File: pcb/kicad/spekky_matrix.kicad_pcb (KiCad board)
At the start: 2 copper layers, 153 x 95.8 mm, 330 parts, among them J1 USB_B_Micro, J2 Conn_ARM_JTAG_SWD_10, Q1 DMP3125L-7, Q2 DMP3125L-7, Q3 DMP3125L-7, Q4 DMP3125L-7, Q5 DMP3125L-7, Q6 DMP3125L-7, Q7 DMP3125L-7, Q8 DMP3125L-7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

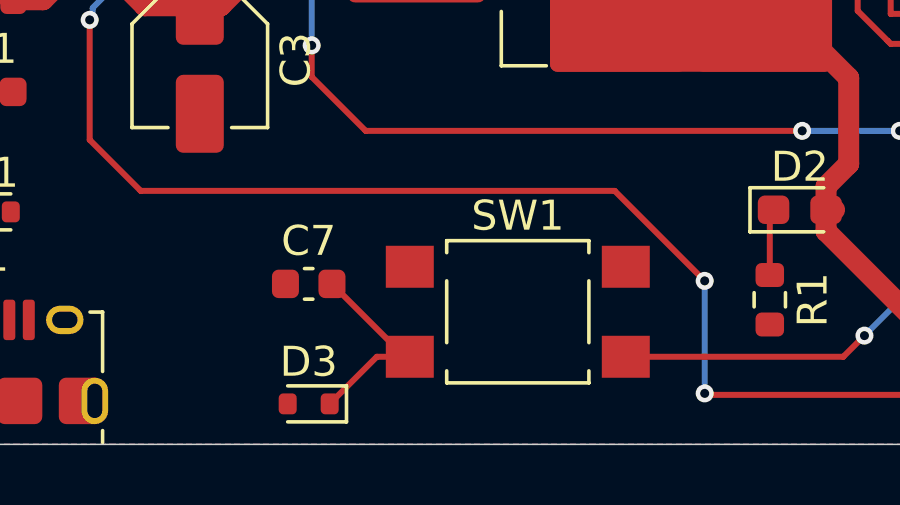
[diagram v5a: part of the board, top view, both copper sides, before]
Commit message: Correct nrst switch connections
- Moved ESD diode and capacitor to remove any stubbing on the
  transmission line
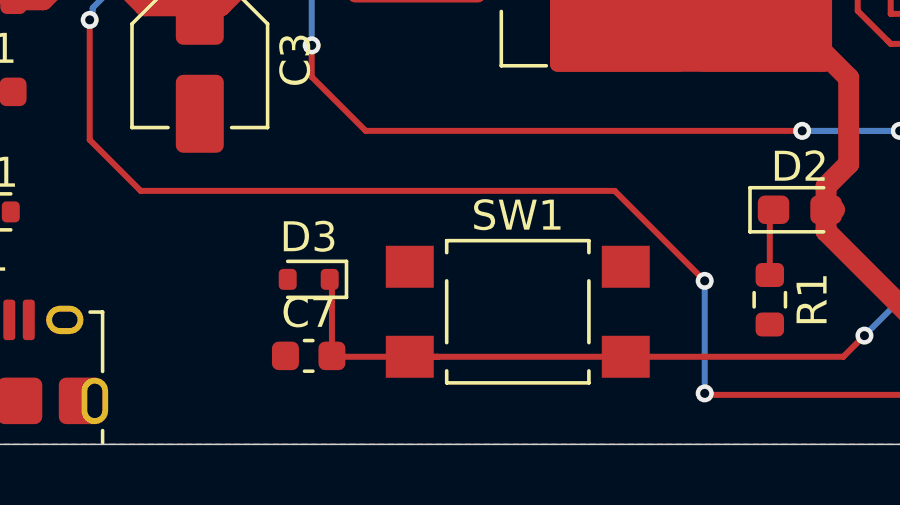
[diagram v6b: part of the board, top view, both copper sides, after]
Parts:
- moved D3 4.15 mm to (86.6, 127.2)
- moved C7 2.40 mm to (86.6, 129.8)
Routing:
- net /STM32 MCU/NRST: track 44.8 -> 51.3 mm
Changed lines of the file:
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@@
 	(footprint "Diode_SMD:D_SOD-523"
 		(layer "F.Cu")
-		(at 86.6 131.4 180)
+		(at 86.6 127.25 180)
 		(descr "http://www.diodes.com/datasheets/ap02001.pdf p.144")
 		(tags "Diode SOD523")
@@
 	(footprint "Capacitor_SMD:C_0603_1608Metric"
 		(layer "F.Cu")
-		(at 86.6 127.4)
+		(at 86.6 129.8)
 		(descr "Capacitor SMD 0603 (1608 Metric), square (rectangular) end terminal, IPC_7351 nominal, (Body size source: IPC-SM-782 page 76, https://www.pcb-3d.com/wordpress/wp-content/uploads/ipc-sm-782a_amendment_1_and_2.pdf), generated with kicad-footprint-generator")
 		(tags "capacitor")
@@
 	)
 	(segment
-		(start 89.97 129.83)
-		(end 88.87 129.83)
-		(width 0.2)
-		(layer "F.Cu")
-		(net 5)
-	)
-	(segment
 		(start 115.95 113.9)
 		(end 115.95 118.5)
@@
 	)
 	(segment
-		(start 88.87 129.83)
-		(end 87.3 131.4)
+		(start 114.267179 121.899231)
+		(end 114.7 122.332052)
 		(width 0.2)
 		(layer "F.Cu")
@@
 	)
 	(segment
-		(start 114.267179 121.899231)
-		(end 114.7 122.332052)
+		(start 87.375 129.83)
+		(end 90.9 129.83)
 		(width 0.2)
 		(layer "F.Cu")
@@
 	)
 	(segment
+		(start 90.9 129.83)
+		(end 97.17 129.83)
+		(width 0.2)
+		(layer "F.Cu")
+		(net 5)
+	)
+	(segment
+		(start 89.97 129.83)
+		(end 90.9 129.83)
+		(width 0.2)
+		(layer "F.Cu")
+		(net 5)
+	)
+	(segment
 		(start 104.42 129.83)
 		(end 97.17 129.83)
@@
 	)
 	(segment
-		(start 87.375 127.4)
-		(end 89.805 129.83)
+		(start 87.375 127.325)
+		(end 87.375 129.83)
+		(width 0.2)
+		(layer "F.Cu")
+		(net 5)
+	)
+	(segment
+		(start 87.3 127.25)
+		(end 87.375 127.325)
 		(width 0.2)
 		(layer "F.Cu")
